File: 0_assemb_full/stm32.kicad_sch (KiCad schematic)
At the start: 19 parts, among them J10 Conn_02x05_Odd_Even, J11 SPIConn_01x03, J9 Conn_01x02, U5 STM32F091RCTx

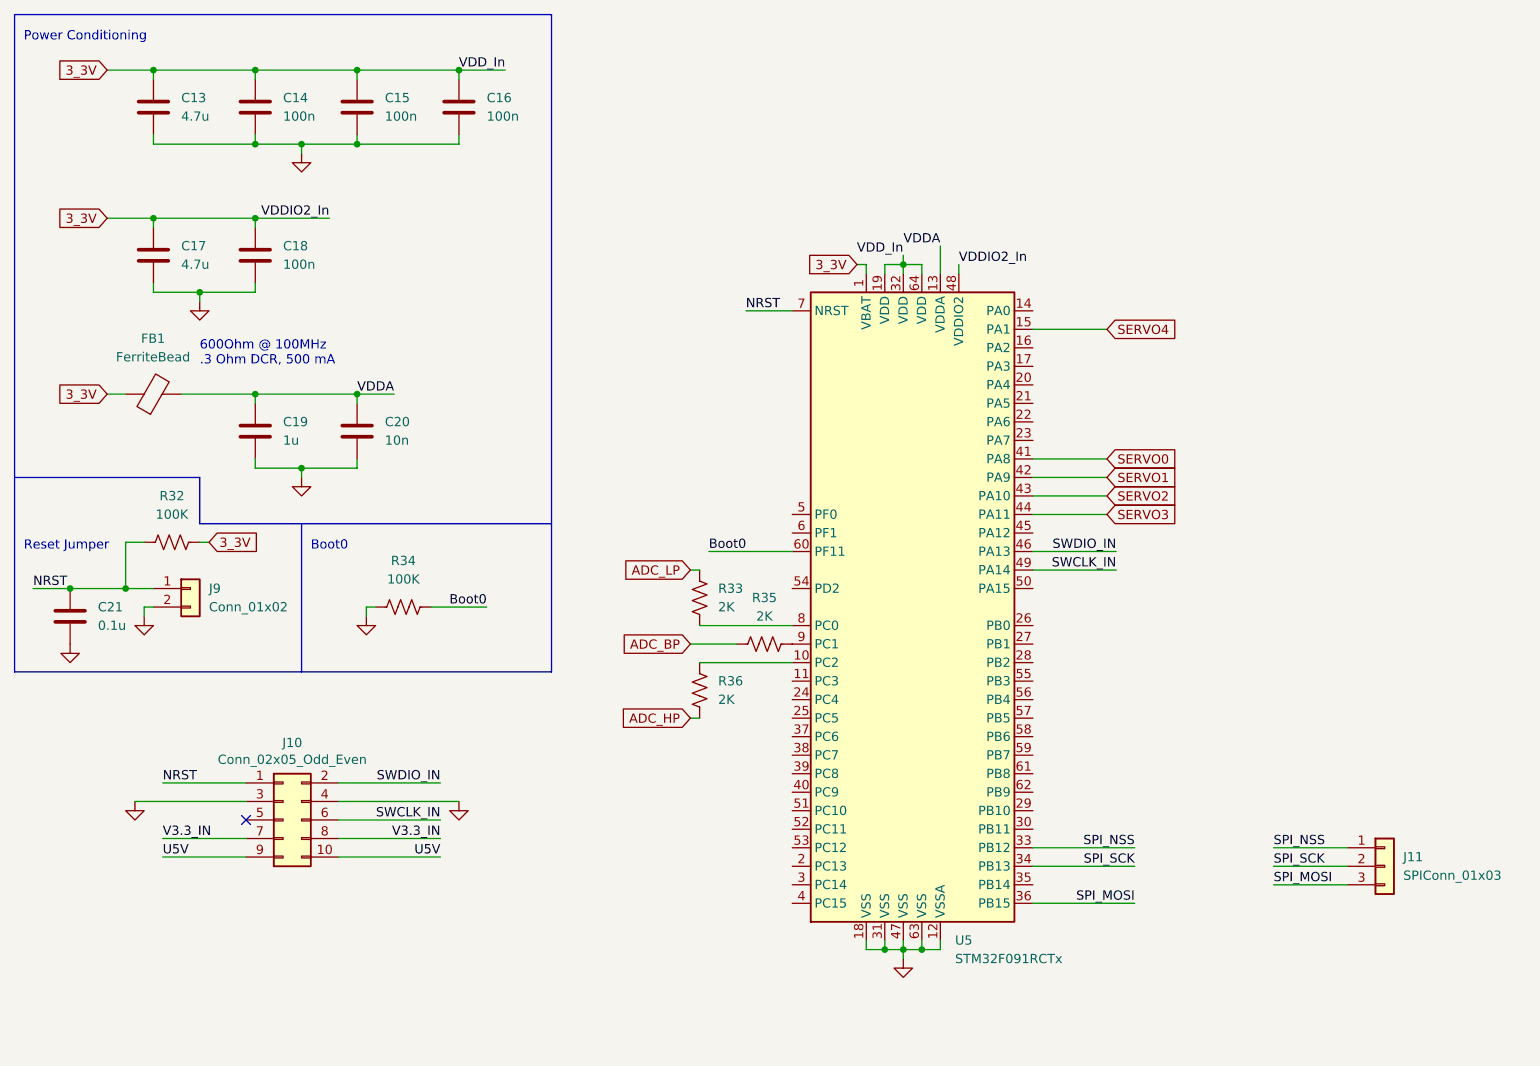
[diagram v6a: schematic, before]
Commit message: A lot of work done on the STM32 PCB layout.
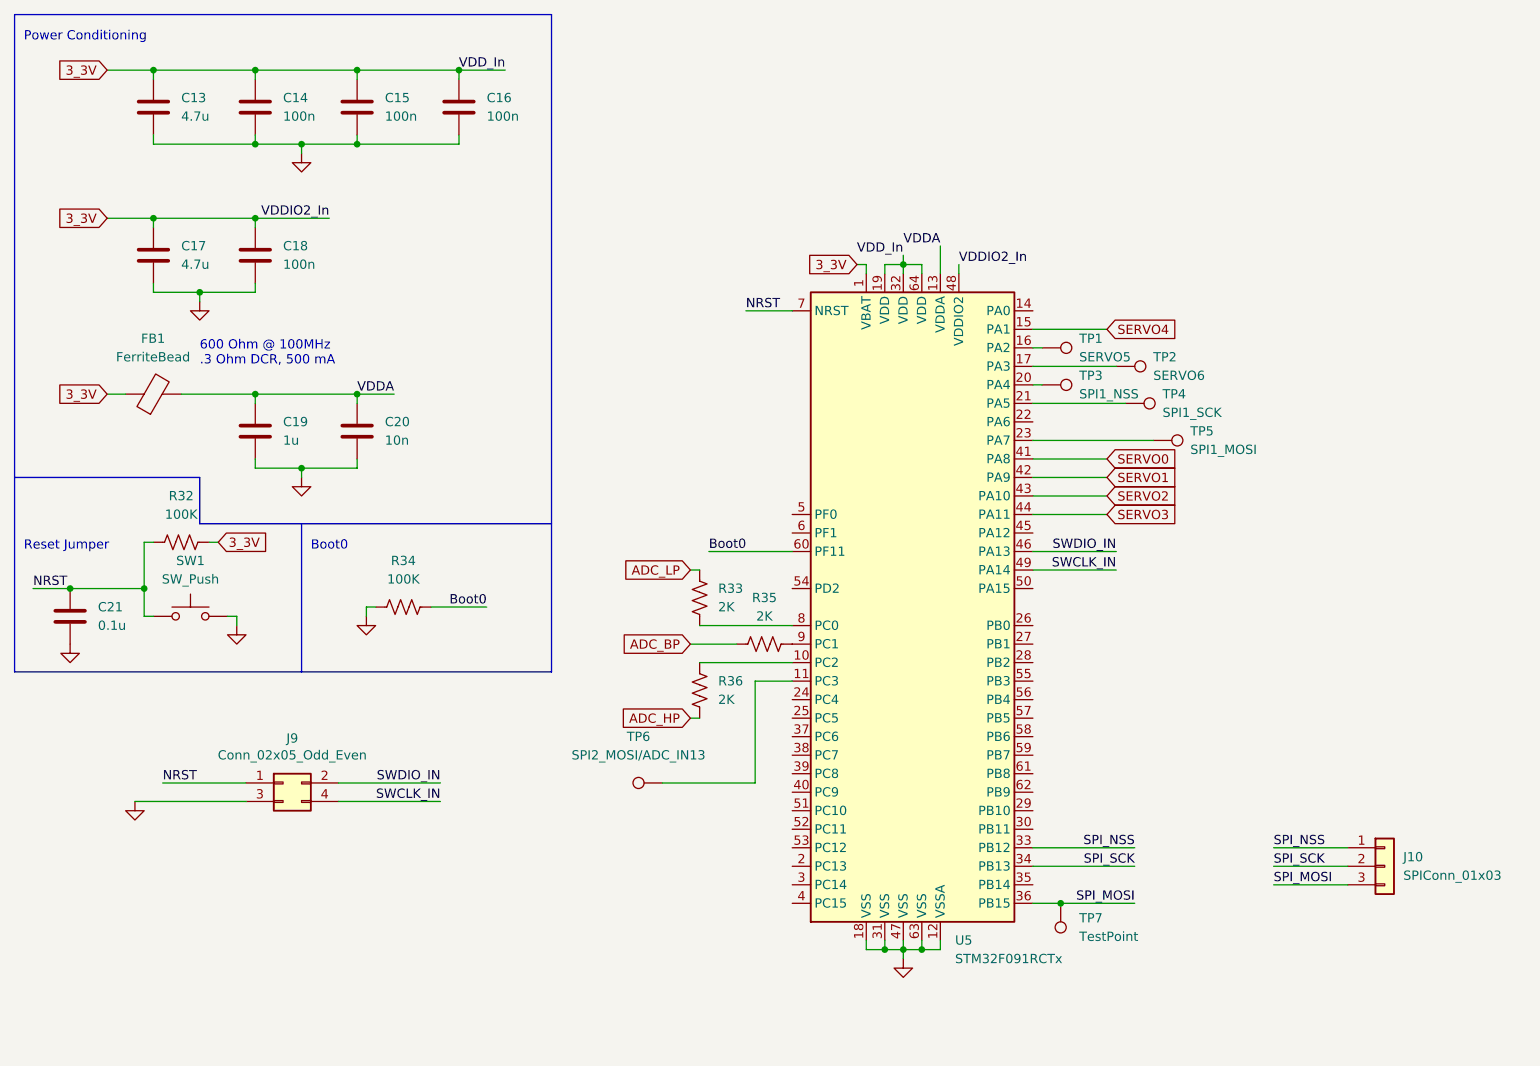
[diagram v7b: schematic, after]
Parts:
- removed J9: Conn_01x02, symbol Connector_Generic:Conn_01x02
- added SW1: SW_Push, Button_Switch_THT:SW_PUSH-12mm_Wuerth-430476085716, symbol Switch:SW_Push
- added TP1: SERVO5, TestPoint:TestPoint_THTPad_1.5x1.5mm_Drill0.7mm, symbol Connector:TestPoint
- added TP2: SERVO6, TestPoint:TestPoint_THTPad_1.5x1.5mm_Drill0.7mm, symbol Connector:TestPoint
- added TP3: SPI1_NSS, TestPoint:TestPoint_THTPad_1.5x1.5mm_Drill0.7mm, symbol Connector:TestPoint
- added TP4: SPI1_SCK, TestPoint:TestPoint_THTPad_1.5x1.5mm_Drill0.7mm, symbol Connector:TestPoint
- added TP5: SPI1_MOSI, TestPoint:TestPoint_THTPad_1.5x1.5mm_Drill0.7mm, symbol Connector:TestPoint
- added TP6: SPI2_MOSI/ADC_IN13, TestPoint:TestPoint_THTPad_1.5x1.5mm_Drill0.7mm, symbol Connector:TestPoint
- added TP7: TestPoint, TestPoint:TestPoint_THTPad_1.5x1.5mm_Drill0.7mm, symbol Connector:TestPoint
- C13, C17, C19: footprint (none) -> Capacitor_THT:CP_Radial_D5.0mm_P2.50mm
- C14, C15, C16, C18, C20, C21: footprint (none) -> Capacitor_SMD:C_0805_2012Metric_Pad1.18x1.45mm_HandSolder
- FB1, R32, R33, R34, R35, R36: footprint (none) -> Resistor_SMD:R_0805_2012Metric_Pad1.20x1.40mm_HandSolder
- J10: renamed from J11; footprint (none) -> Connector_PinSocket_2.54mm:PinSocket_1x03_P2.54mm_Vertical
- J9: renamed from J10; footprint Connector_IDC:IDC-Header_2x05_P2.54mm_Vertical -> Connector_PinHeader_2.54mm:PinHeader_2x02_P2.54mm_Vertical; symbol Connector_Generic:Conn_02x05_Odd_Even -> Connector_Generic:Conn_02x02_Odd_Even
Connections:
- net GND: now also SW1.2; no longer J9.4 (Pin_4)
- net NRST: now also SW1.1
- net SPI_MOSI: now also TP7.1
- net SWCLK_IN: now also J9.4 (Pin_4); no longer J9.6 (Pin_6)
- net at U5.11 (PC3): now also TP6.1
- net at U5.16 (PA2): now also TP1.1
- net at U5.17 (PA3): now also TP2.1
- net at U5.20 (PA4): now also TP3.1
- net at U5.21 (PA5): now also TP4.1
- net at U5.23 (PA7): now also TP5.1
- removed net U5V: J9.10 (Pin_10), J9.9 (Pin_9)
- removed net V3.3_IN: J9.7 (Pin_7), J9.8 (Pin_8)
- no-connect marks 1 -> 0
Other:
- note added: "600 Ohm @ 100MHz .3 Ohm DCR, 500 mA"
- note removed: "600Ohm @ 100MHz .3 Ohm DCR, 500 mA"
- moved on the sheet: R32

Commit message: Pre-STM32 portion rework
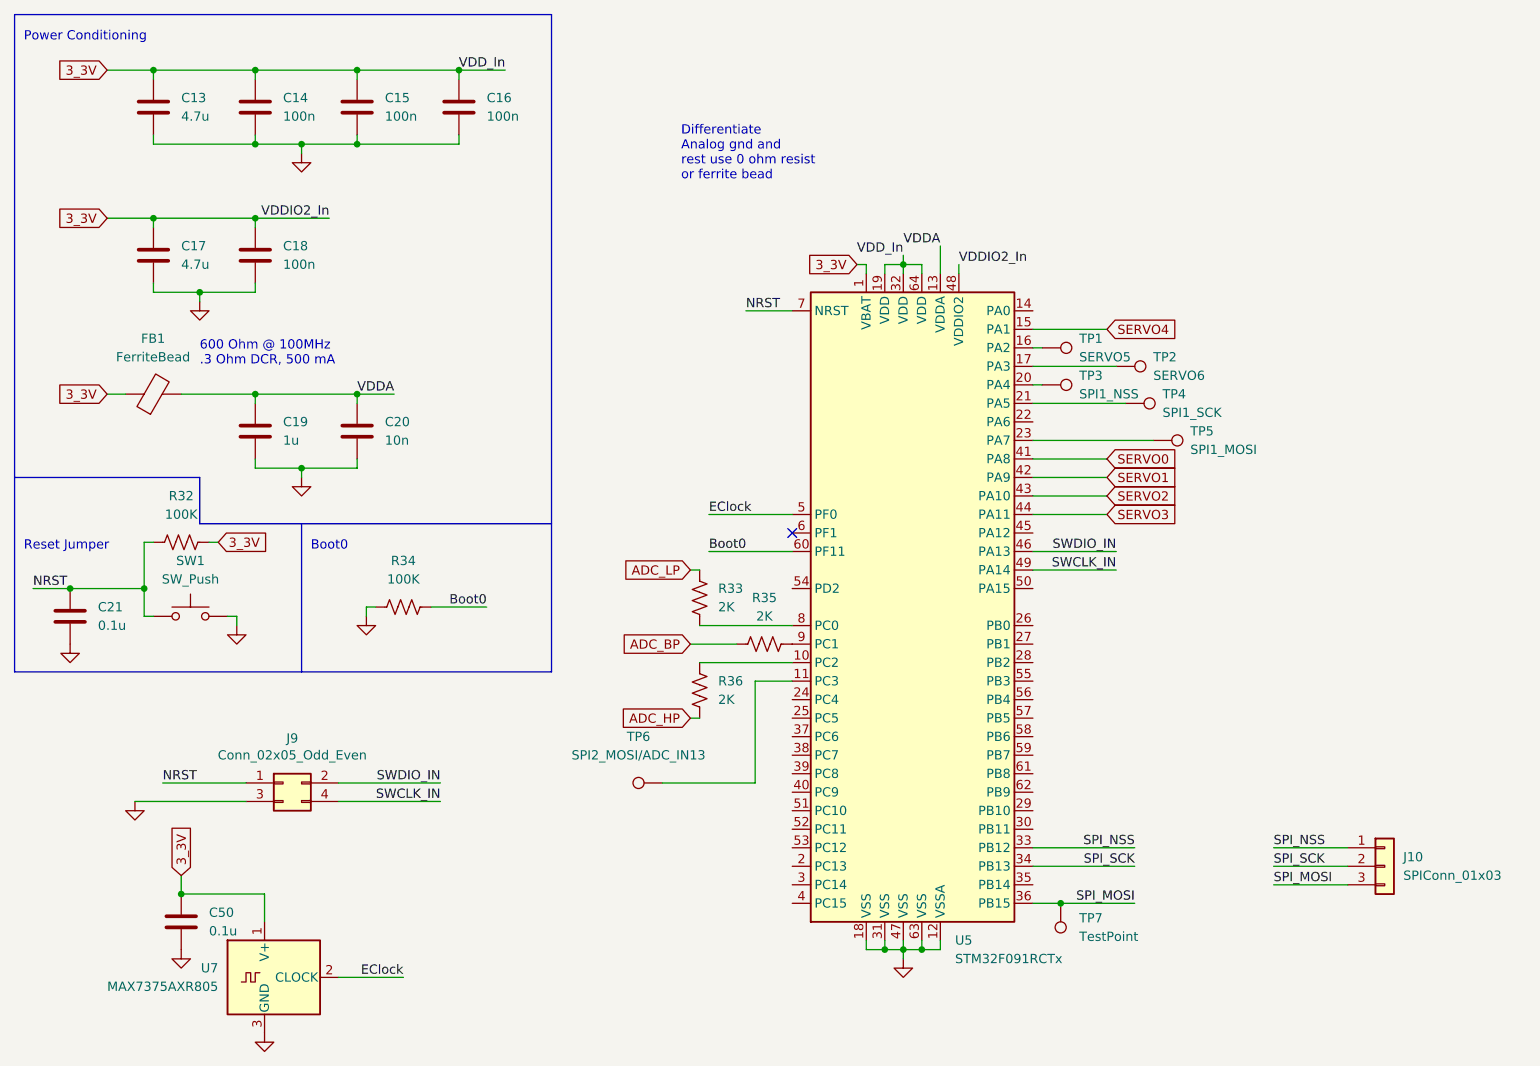
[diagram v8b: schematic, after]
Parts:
- added C50: 0.1u, Capacitor_SMD:C_0805_2012Metric_Pad1.18x1.45mm_HandSolder, symbol Device:C
- added U7: MAX7375AXR805, Package_TO_SOT_SMD:SOT-323_SC-70, symbol Oscillator:MAX7375AXR805
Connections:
- net 3_3V: now also C50.1, U7.1 (V+)
- net GND: now also C50.2, U7.3 (GND)
- net EClock: now reaches U5.5 (PF0)
- net EClock: now also U7.2 (CLOCK)
- no-connect marks 0 -> 1
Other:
- note added: "Differentiate Analog gnd and rest use 0 ohm resist or ferrite bead"
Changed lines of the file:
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@@
   (junction (at 45.72 40.64) (diameter 0) (color 0 0 0 0)
   )
+  (junction (at 35.56 133.35) (diameter 0) (color 0 0 0 0)
+  )
   (junction (at 134.62 140.97) (diameter 0) (color 0 0 0 0)
   )
@@
   (junction (at 30.48 91.44) (diameter 0) (color 0 0 0 0)
   )
+  (no_connect (at 119.38 83.82))
   (polyline (pts (xy 12.7 12.7) (xy 86.36 12.7))
     (stroke (width 0) (type default) (color 0 0 0 0))
@@
     (stroke (width 0) (type default) (color 0 0 0 0))
   )
+  (wire (pts (xy 35.56 133.35) (xy 46.99 133.35))
+    (stroke (width 0) (type default) (color 0 0 0 0))
+  )
   (wire (pts (xy 134.62 45.72) (xy 134.62 46.99))
     (stroke (width 0) (type default) (color 0 0 0 0))
@@
     (stroke (width 0) (type default) (color 0 0 0 0))
   )
+  (wire (pts (xy 107.95 81.28) (xy 119.38 81.28))
+    (stroke (width 0) (type default) (color 0 0 0 0))
+  )
   (polyline (pts (xy 12.7 76.2) (xy 38.1 76.2))
     (stroke (width 0) (type default) (color 0 0 0 0))
@@
     (stroke (width 0) (type default) (color 0 0 0 0))
   )
+  (wire (pts (xy 46.99 133.35) (xy 46.99 137.16))
+    (stroke (width 0) (type default) (color 0 0 0 0))
+  )
   (wire (pts (xy 45.72 29.21) (xy 45.72 30.48))
     (stroke (width 0) (type default) (color 0 0 0 0))
@@
     (stroke (width 0) (type default) (color 0 0 0 0))
   )
+  (wire (pts (xy 35.56 130.81) (xy 35.56 133.35))
+    (stroke (width 0) (type default) (color 0 0 0 0))
+  )
   (wire (pts (xy 45.72 41.91) (xy 45.72 40.64))
     (stroke (width 0) (type default) (color 0 0 0 0))
@@
     (stroke (width 0) (type default) (color 0 0 0 0))
   )
+  (wire (pts (xy 57.15 144.78) (xy 66.04 144.78))
+    (stroke (width 0) (type default) (color 0 0 0 0))
+  )
   (wire (pts (xy 105.41 88.9) (xy 106.68 88.9))
     (stroke (width 0) (type default) (color 0 0 0 0))
   )
+  (text "Differentiate\nAnalog gnd and\nrest use 0 ohm resist\nor ferrite bead"
+    (at 104.14 35.56 0)
+    (effects (font (size 1.27 1.27)) (justify left bottom))
+  )
   (text "600 Ohm @ 100MHz\n.3 Ohm DCR, 500 mA" (at 38.1 60.96 0)
     (effects (font (size 1.27 1.27)) (justify left bottom))
@@
     (effects (font (size 1.27 1.27)) (justify right bottom))
   )
+  (label "EClock" (at 66.04 144.78 180)
+    (effects (font (size 1.27 1.27)) (justify right bottom))
+  )
   (label "SWDIO_IN" (at 163.83 86.36 180)
     (effects (font (size 1.27 1.27)) (justify right bottom))
@@
   (label "VDDA" (at 139.7 44.45 180)
     (effects (font (size 1.27 1.27)) (justify right bottom))
+  )
+  (label "EClock" (at 107.95 81.28 0)
+    (effects (font (size 1.27 1.27)) (justify left bottom))
   )
   (label "VDDIO2_In" (at 142.24 46.99 0)
@@
     )
   )
+  (global_label "3_3V" (shape input) (at 35.56 130.81 90) (fields_autoplaced)
+    (effects (font (size 1.27 1.27)) (justify left))
+    (property "Intersheet References" "${INTERSHEET_REFS}" (id 0) (at 35.4806 123.9217 90)
+      (effects (font (size 1.27 1.27)) (justify left) hide)
+    )
+  )
   (global_label "ADC_HP" (shape input) (at 105.41 109.22 180) (fields_autoplaced)
     (effects (font (size 1.27 1.27)) (justify right))
@@
       (effects (font (size 1.27 1.27)) (justify right) hide)
     )
+  )
+  (symbol (lib_id "power:GND") (at 46.99 152.4 0) (unit 1)
+    (in_bom yes) (on_board yes)
+    (property "Reference" "#PWR045" (id 0) (at 46.99 158.75 0)
+      (effects (font (size 1.27 1.27)) hide)
+    )
+    (property "Value" "GND" (id 1) (at 47.117 156.7942 0)
+      (effects (font (size 1.27 1.27)) hide)
+    )
+    (property "Footprint" "" (id 2) (at 46.99 152.4 0)
+      (effects (font (size 1.27 1.27)) hide)
+    )
+    (property "Datasheet" "" (id 3) (at 46.99 152.4 0)
+      (effects (font (size 1.27 1.27)) hide)
+    )
+    (pin "1")
   )
   (symbol (lib_id "Connector:TestPoint") (at 163.83 60.96 270) (unit 1)
@@
     (pin "4")
   )
+  (symbol (lib_id "power:GND") (at 35.56 140.97 0) (unit 1)
+    (in_bom yes) (on_board yes)
+    (property "Reference" "#PWR024" (id 0) (at 35.56 147.32 0)
+      (effects (font (size 1.27 1.27)) hide)
+    )
+    (property "Value" "GND" (id 1) (at 35.687 145.3642 0)
+      (effects (font (size 1.27 1.27)) hide)
+    )
+    (property "Footprint" "" (id 2) (at 35.56 140.97 0)
+      (effects (font (size 1.27 1.27)) hide)
+    )
+    (property "Datasheet" "" (id 3) (at 35.56 140.97 0)
+      (effects (font (size 1.27 1.27)) hide)
+    )
+    (pin "1")
+  )
   (symbol (lib_id "Device:C") (at 59.69 69.85 0) (unit 1)
     (in_bom yes) (on_board yes) (fields_autoplaced)
@@
     (pin "1")
     (pin "2")
+  )
+  (symbol (lib_id "Oscillator:MAX7375AXR805") (at 46.99 144.78 0) (unit 1)
+    (in_bom yes) (on_board yes) (fields_autoplaced)
+    (property "Reference" "U7" (id 0) (at 40.64 143.5099 0)
+      (effects (font (size 1.27 1.27)) (justify right))
+    )
+    (property "Value" "MAX7375AXR805" (id 1) (at 40.64 146.0499 0)
+      (effects (font (size 1.27 1.27)) (justify right))
+    )
+    (property "Footprint" "Package_TO_SOT_SMD:SOT-323_SC-70" (id 2) (at 74.93 153.67 0)
+      (effects (font (size 1.27 1.27)) hide)
+    )
+    (property "Datasheet" "https://datasheets.maximintegrated.com/en/ds/MAX7375.pdf" (id 3) (at 44.45 144.78 0)
+      (effects (font (size 1.27 1.27)) hide)
+    )
+    (pin "1")
+    (pin "2")
+    (pin "3")
   )
   (symbol (lib_id "Device:R_US") (at 106.68 105.41 180) (unit 1)
@@
     (pin "1")
   )
+  (symbol (lib_id "Device:C") (at 35.56 137.16 0) (unit 1)
+    (in_bom yes) (on_board yes) (fields_autoplaced)
+    (property "Reference" "C50" (id 0) (at 39.37 135.8899 0)
+      (effects (font (size 1.27 1.27)) (justify left))
+    )
+    (property "Value" "0.1u" (id 1) (at 39.37 138.4299 0)
+      (effects (font (size 1.27 1.27)) (justify left))
+    )
+    (property "Footprint" "Capacitor_SMD:C_0805_2012Metric_Pad1.18x1.45mm_HandSolder" (id 2) (at 36.5252 140.97 0)
+      (effects (font (size 1.27 1.27)) hide)
+    )
+    (property "Datasheet" "~" (id 3) (at 35.56 137.16 0)
+      (effects (font (size 1.27 1.27)) hide)
+    )
+    (pin "1")
+    (pin "2")
+  )
   (symbol (lib_id "Device:C") (at 45.72 25.4 0) (unit 1)
